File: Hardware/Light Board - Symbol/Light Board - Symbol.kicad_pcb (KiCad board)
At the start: 2 copper layers, 81.4 x 81.4 mm, 19 parts, among them J1 V+, J2 V-

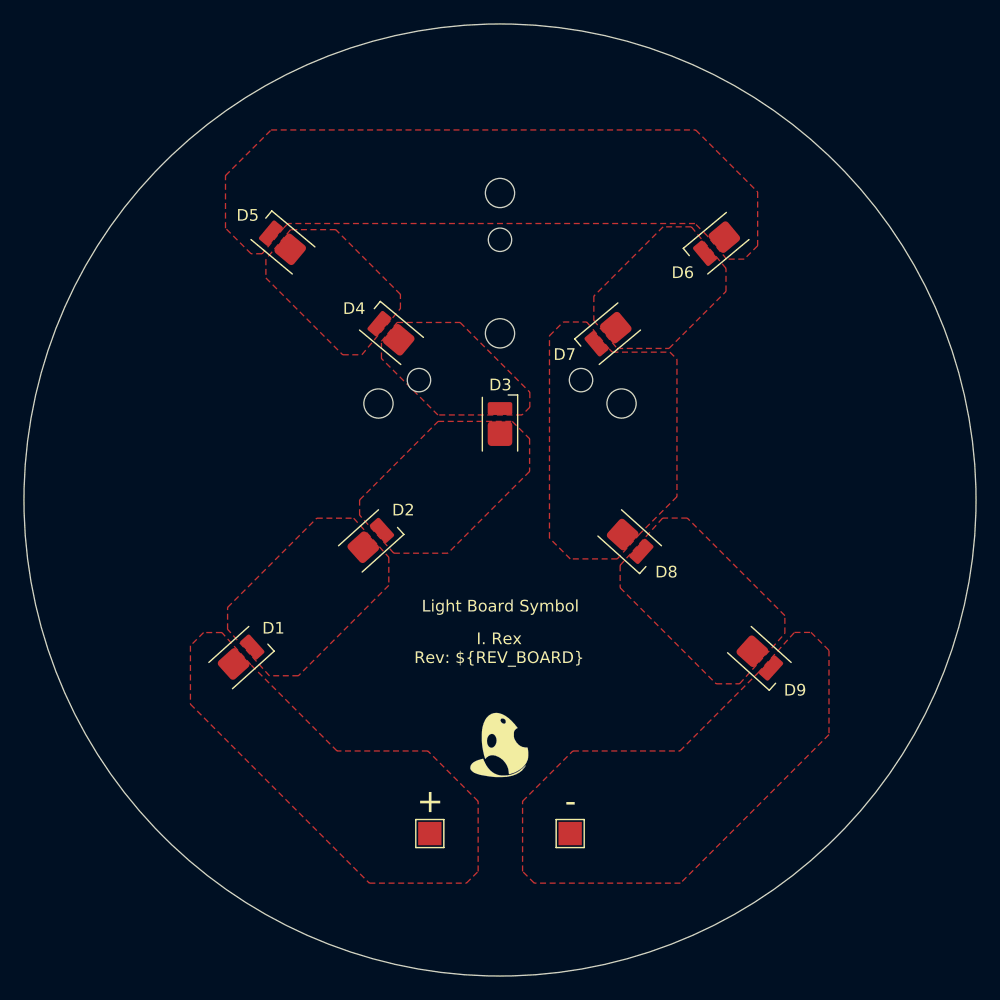
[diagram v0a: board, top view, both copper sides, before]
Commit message: Added LED library and fixed orientation
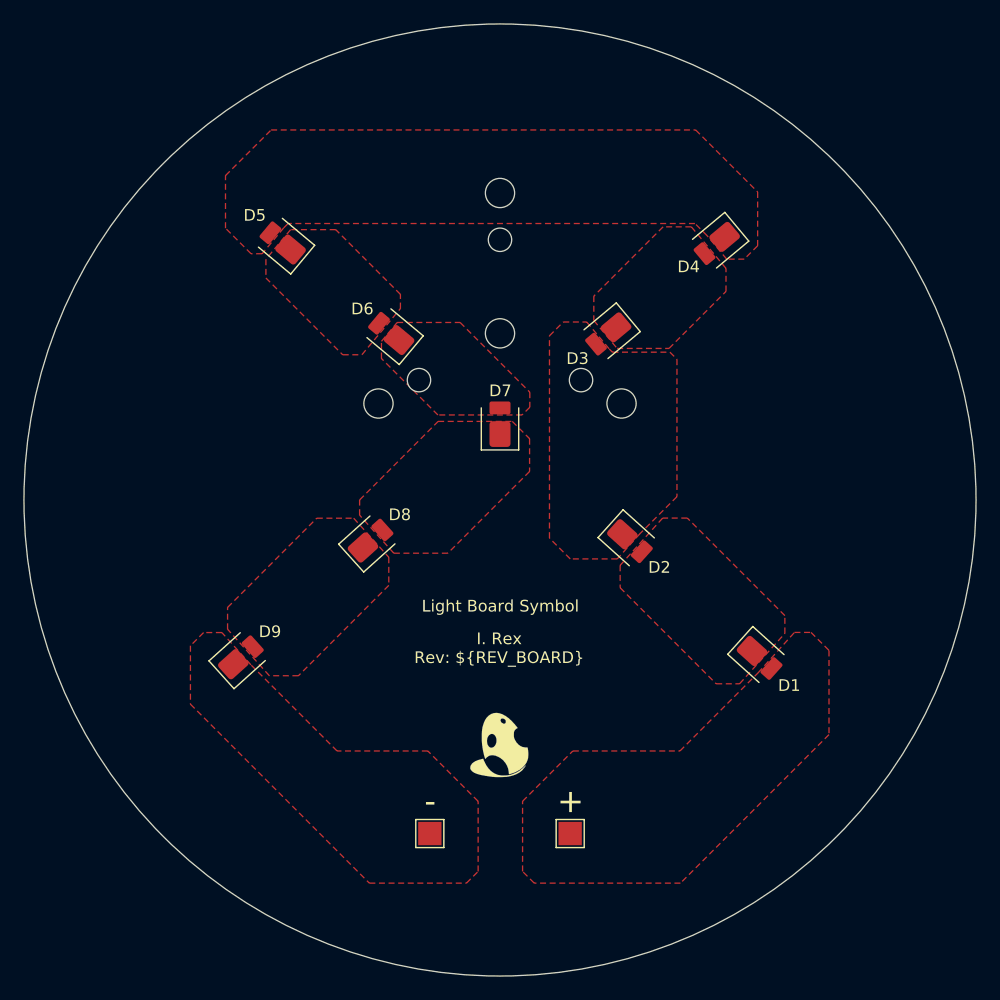
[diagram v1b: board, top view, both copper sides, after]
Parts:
- D1: renamed from D9; footprint LED_SMD:LED_Everlight-SMD3528_3.5x2.8mm_67-21ST -> irex_LED_SMD:LED_Cree_J-Series_SMD2835_2.8x3.5mm
- D2: renamed from D8; footprint LED_SMD:LED_Everlight-SMD3528_3.5x2.8mm_67-21ST -> irex_LED_SMD:LED_Cree_J-Series_SMD2835_2.8x3.5mm
- D3: renamed from D7; footprint LED_SMD:LED_Everlight-SMD3528_3.5x2.8mm_67-21ST -> irex_LED_SMD:LED_Cree_J-Series_SMD2835_2.8x3.5mm
- D4: renamed from D6; footprint LED_SMD:LED_Everlight-SMD3528_3.5x2.8mm_67-21ST -> irex_LED_SMD:LED_Cree_J-Series_SMD2835_2.8x3.5mm
- D5: footprint LED_SMD:LED_Everlight-SMD3528_3.5x2.8mm_67-21ST -> irex_LED_SMD:LED_Cree_J-Series_SMD2835_2.8x3.5mm
- D6: renamed from D4; footprint LED_SMD:LED_Everlight-SMD3528_3.5x2.8mm_67-21ST -> irex_LED_SMD:LED_Cree_J-Series_SMD2835_2.8x3.5mm
- D7: renamed from D3; footprint LED_SMD:LED_Everlight-SMD3528_3.5x2.8mm_67-21ST -> irex_LED_SMD:LED_Cree_J-Series_SMD2835_2.8x3.5mm
- D8: renamed from D2; footprint LED_SMD:LED_Everlight-SMD3528_3.5x2.8mm_67-21ST -> irex_LED_SMD:LED_Cree_J-Series_SMD2835_2.8x3.5mm
- D9: renamed from D1; footprint LED_SMD:LED_Everlight-SMD3528_3.5x2.8mm_67-21ST -> irex_LED_SMD:LED_Cree_J-Series_SMD2835_2.8x3.5mm
- J1: renamed from J2; value V- -> V+
- J2: renamed from J1; value V+ -> V-
- turned D1 to -41.982 degrees
- turned D2 to -41.982 degrees
- turned D3 to -140.175 degrees
- turned D4 to -140.175 degrees
- turned D5 to 140.175 degrees
- turned D6 to 140.175 degrees
- turned D7 to 90 degrees
- turned D8 to 41.982 degrees
- turned D9 to 41.982 degrees
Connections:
- D1 pad 1: /V- -> /K_D1
- D1 pad 2: /K_D8 -> /V+
- D2 pad 1: /K_D8 -> /K_D2
- D2 pad 2: /K_D7 -> /K_D1
- D3 pad 1: /K_D7 -> /K_D3
- D3 pad 2: /K_D6 -> /K_D2
- D4 pad 1: /K_D6 -> /K_D4
- D4 pad 2: /K_D5 -> /K_D3
- D6 pad 1: /K_D4 -> /K_D6
- D6 pad 2: /K_D3 -> /K_D5
- D7 pad 1: /K_D3 -> /K_D7
- D7 pad 2: /K_D2 -> /K_D6
- D8 pad 1: /K_D2 -> /K_D8
- D8 pad 2: /K_D1 -> /K_D7
- D9 pad 1: /K_D1 -> /V-
- D9 pad 2: /V+ -> /K_D8
- J1 pad 1: /V- -> /V+
- J2 pad 1: /V+ -> /V-
